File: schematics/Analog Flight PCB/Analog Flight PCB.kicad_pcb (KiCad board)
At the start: 2 copper layers, 77 parts, among them J1 Screw_Terminal_01x02, J10 Conn_01x02_Male, J2 Screw_Terminal_01x03, J3 Screw_Terminal_01x04, J4 Screw_Terminal_01x02, J5 Screw_Terminal_01x02, J6 Screw_Terminal_01x02, J7 Screw_Terminal_01x02, J8 Screw_Terminal_01x02, J9 Conn_02x06_Top_Bottom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

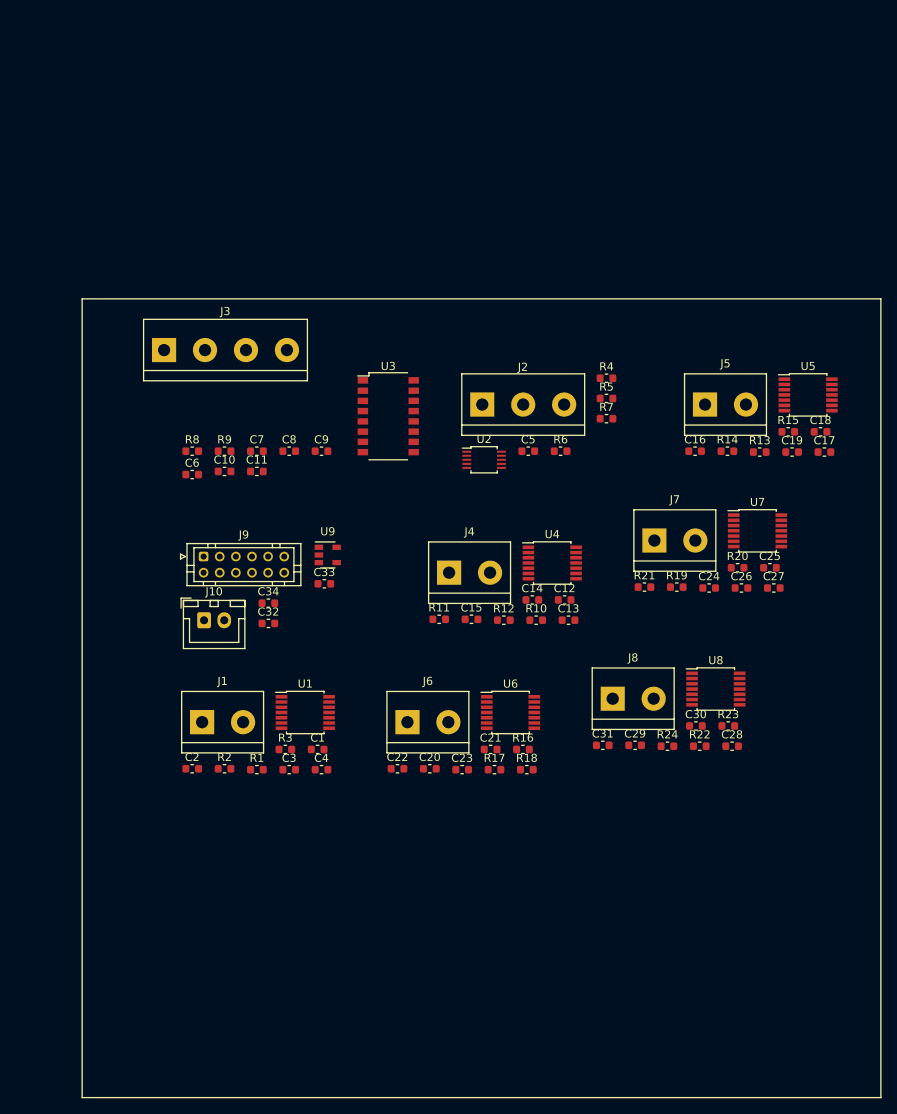
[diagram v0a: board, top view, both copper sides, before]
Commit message: Separated all components to make traces easier.
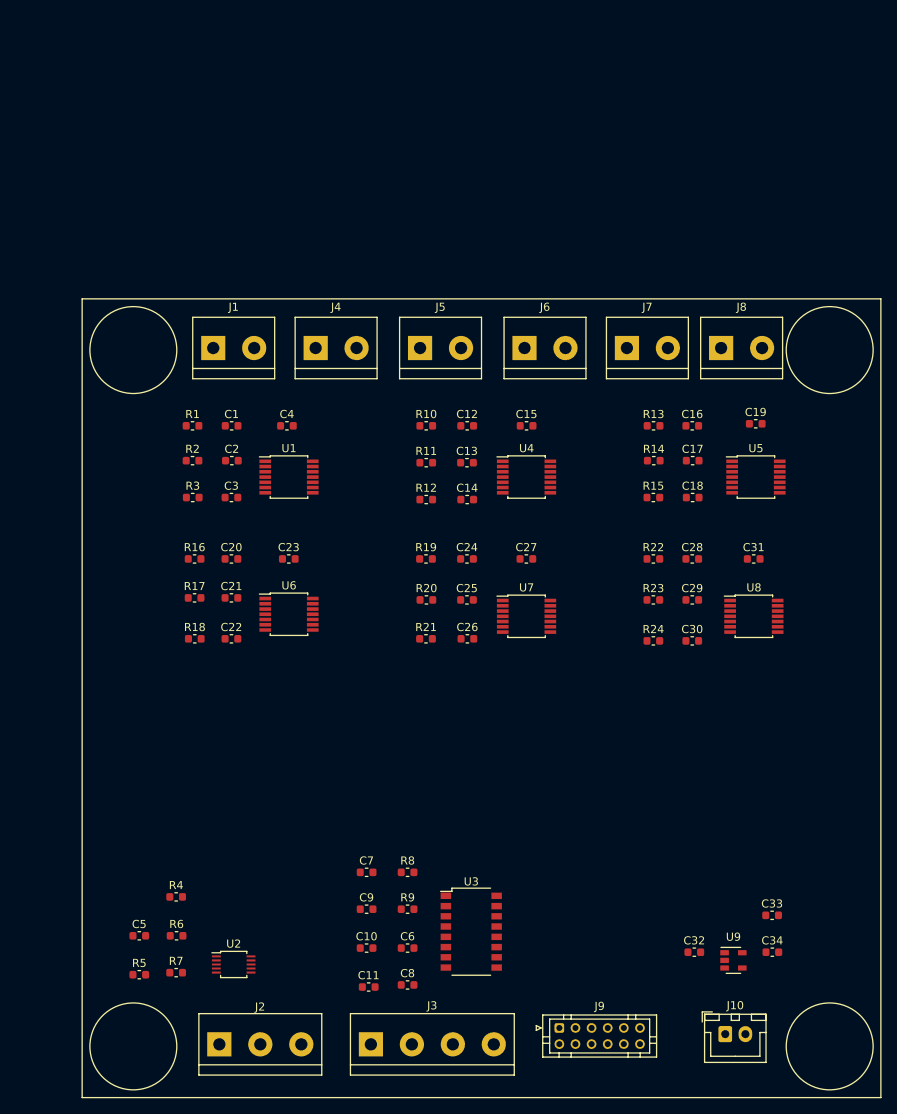
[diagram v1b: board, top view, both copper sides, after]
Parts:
- moved R5 92.0 mm to (108.7, 147.3)
- moved J3 89.8 mm to (137.4, 156.0)
- moved R7 87.0 mm to (113.3, 147.1)
- moved J2 85.8 mm to (118.6, 156.0)
- moved R4 83.6 mm to (113.3, 137.7)
- moved J10 82.5 mm to (181.4, 154.7)
- moved C5 77.1 mm to (108.7, 142.5)
- moved R6 76.7 mm to (113.3, 142.5)
- moved C34 76.0 mm to (187.2, 144.5)
- moved J9 73.2 mm to (160.8, 153.9)
- moved U9 71.1 mm to (182.4, 145.5)
- moved U2 69.9 mm to (120.4, 146.1)
- moved C33 69.1 mm to (187.2, 140.0)
- moved C8 67.8 mm to (142.0, 148.6)
- moved C32 66.7 mm to (177.5, 144.5)
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
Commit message: Changed screw terminals to JST connectors and added two more connectors to the PTs.
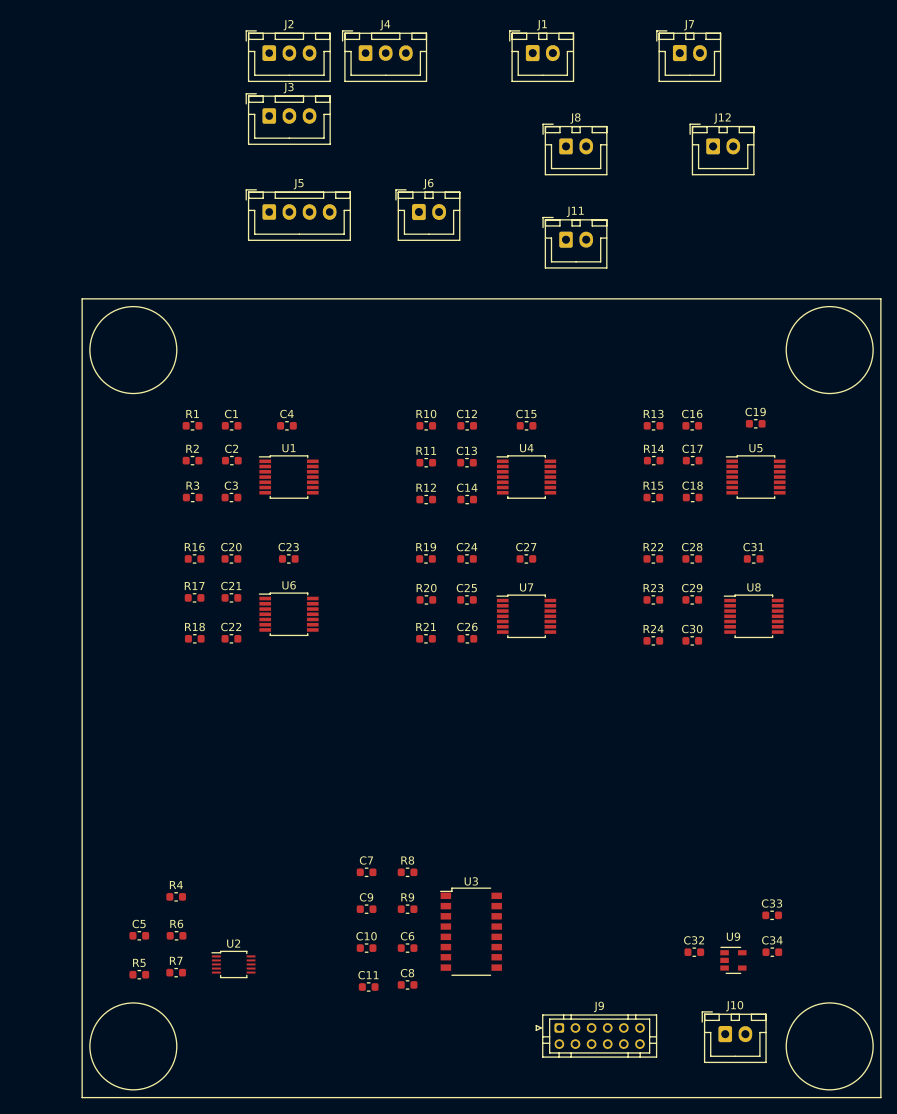
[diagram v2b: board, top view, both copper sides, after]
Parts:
- added J11: Conn_01x02_Male, Connector_JST:JST_XH_B2B-XH-A_1x02_P2.50mm_Vertical, F.Cu at (161.6, 56.2)
- added J12: Conn_01x02_Male, Connector_JST:JST_XH_B2B-XH-A_1x02_P2.50mm_Vertical, F.Cu at (179.8, 44.6)
- J1, J6, J7, J8: value Screw_Terminal_01x02 -> Conn_01x02_Male; footprint TerminalBlock:TerminalBlock_bornier-2_P5.08mm -> Connector_JST:JST_XH_B2B-XH-A_1x02_P2.50mm_Vertical
- J2: value Screw_Terminal_01x03 -> Conn_01x03_Male; footprint TerminalBlock:TerminalBlock_bornier-3_P5.08mm -> Connector_JST:JST_XH_B3B-XH-A_1x03_P2.50mm_Vertical
- J3: value Screw_Terminal_01x04 -> Conn_01x03_Male; footprint TerminalBlock:TerminalBlock_bornier-4_P5.08mm -> Connector_JST:JST_XH_B3B-XH-A_1x03_P2.50mm_Vertical
- J4: value Screw_Terminal_01x02 -> Conn_01x03_Male; footprint TerminalBlock:TerminalBlock_bornier-2_P5.08mm -> Connector_JST:JST_XH_B3B-XH-A_1x03_P2.50mm_Vertical
- J5: value Screw_Terminal_01x02 -> Conn_01x04_Male; footprint TerminalBlock:TerminalBlock_bornier-2_P5.08mm -> Connector_JST:JST_XH_B4B-XH-A_1x04_P2.50mm_Vertical
- moved J2 123.1 mm to (124.8, 33.0)
- moved J3 115.8 mm to (124.8, 40.8)
- moved J1 53.9 mm to (157.5, 33.0)
- moved J7 37.2 mm to (175.7, 33.0)
- moved J4 37.1 mm to (136.8, 33.0)
- moved J8 31.5 mm to (161.6, 44.6)
- moved J5 25.2 mm to (124.8, 52.7)
- moved J6 21.4 mm to (143.4, 52.7)
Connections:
- J3 pad 1: Net-(C11-Pad1) -> Net-(J2-Pad1)
- J3 pad 2: Net-(J3-Pad2) -> Net-(J2-Pad2)
- J3 pad 3: Net-(J3-Pad3) -> Net-(J2-Pad3)
- J4 pad 1: Net-(J4-Pad1) -> Net-(J2-Pad1)
- J4 pad 2: Net-(J4-Pad2) -> Net-(J2-Pad2)
- J5 pad 1: Net-(J5-Pad1) -> Net-(C11-Pad1)
- R10 pad 1: Net-(J4-Pad1) -> Net-(J6-Pad1)
- R11 pad 2: Net-(J4-Pad2) -> Net-(J6-Pad2)
- R12 pad 2: Net-(J4-Pad2) -> Net-(J6-Pad2)
- R13 pad 1: Net-(J5-Pad1) -> Net-(J7-Pad1)
- R14 pad 2: Net-(J5-Pad2) -> Net-(J7-Pad2)
- R15 pad 2: Net-(J5-Pad2) -> Net-(J7-Pad2)
- R16 pad 1: Net-(J6-Pad1) -> Net-(J8-Pad1)
- R17 pad 2: Net-(J6-Pad2) -> Net-(J8-Pad2)
- R18 pad 2: Net-(J6-Pad2) -> Net-(J8-Pad2)
- R19 pad 1: Net-(J7-Pad1) -> Net-(J11-Pad1)
- R20 pad 2: Net-(J7-Pad2) -> Net-(J11-Pad2)
- R21 pad 2: Net-(J7-Pad2) -> Net-(J11-Pad2)
- R22 pad 1: Net-(J8-Pad1) -> Net-(J12-Pad1)
- R23 pad 2: Net-(J8-Pad2) -> Net-(J12-Pad2)
- R24 pad 2: Net-(J8-Pad2) -> Net-(J12-Pad2)
- R8 pad 2: Net-(J3-Pad2) -> Net-(J5-Pad2)
- R9 pad 2: Net-(J3-Pad3) -> Net-(J5-Pad3)

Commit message: Finished layout for individual components and prepping for I2C and power connections.
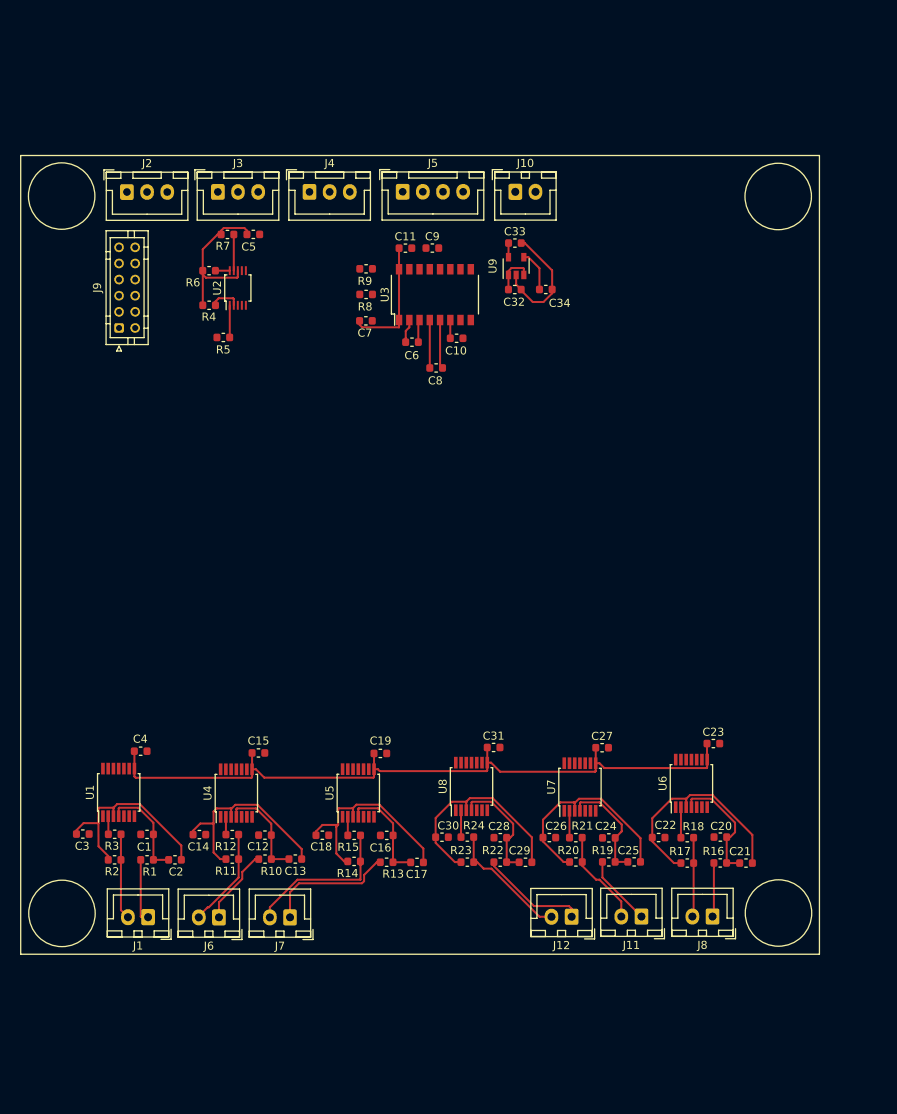
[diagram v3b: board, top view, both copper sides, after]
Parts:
- moved J7 117.6 mm to (127.4, 140.2), turned to 180 degrees
- moved J1 117.3 mm to (109.8, 140.2), turned to 180 degrees
- moved J10 107.7 mm to (155.3, 50.2)
- moved J9 102.6 mm to (106.2, 67.1), turned to 90 degrees
- moved J8 97.2 mm to (179.8, 140.1), turned to 180 degrees
- moved J12 97.1 mm to (162.3, 140.1), turned to 180 degrees
- moved R7 91.8 mm to (119.6, 55.5)
- moved C11 91.7 mm to (141.7, 57.2)
- moved J6 90.9 mm to (118.6, 140.2), turned to 180 degrees
- moved U9 90.2 mm to (155.4, 59.4), turned to 90 degrees
- moved C33 89.3 mm to (155.3, 56.6)
- moved C5 88.1 mm to (122.8, 55.5)
- moved C34 86.9 mm to (159.1, 62.3)
- moved C32 85.1 mm to (155.3, 62.3)
- moved J11 84.5 mm to (171.0, 140.1), turned to 180 degrees
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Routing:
- net +3V3: track 0.00 -> 112.3 mm
- net Net-(C21-Pad2): track 0.00 -> 27.8 mm
- net Net-(C17-Pad2): track 0.00 -> 26.9 mm
- net Net-(C29-Pad2): track 0.00 -> 26.4 mm
- net Net-(C25-Pad2): track 0.00 -> 26.2 mm
- net Net-(C13-Pad2): track 0.00 -> 26.2 mm
- net Net-(C2-Pad2): track 0.00 -> 25.9 mm
- net Net-(J7-Pad2): track 0.00 -> 19.4 mm
- net Net-(J7-Pad1): track 0.00 -> 16.4 mm
- net Net-(J12-Pad2): track 0.00 -> 15.6 mm
- net Net-(C11-Pad1): track 0.00 -> 15.3 mm
- net GND: track 0.00 -> 15.1 mm
- net Net-(C20-Pad2): track 0.00 -> 15.0 mm
- net Net-(C28-Pad2): track 0.00 -> 14.2 mm
- net Net-(C24-Pad2): track 0.00 -> 13.9 mm
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
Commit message: Preliminary PCB design for Analog Flight Board completed. Needs further review.
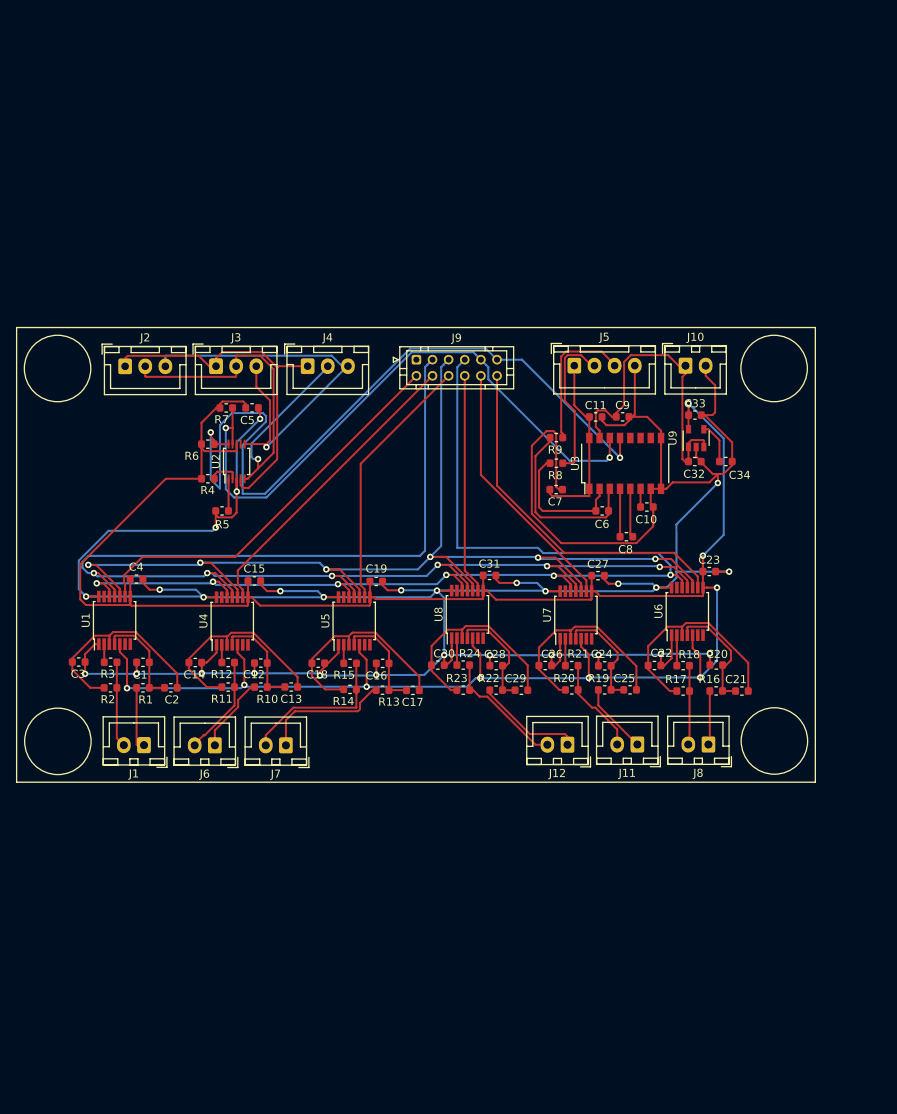
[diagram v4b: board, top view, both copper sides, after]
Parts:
- moved J9 37.1 mm to (143.1, 71.0), turned to 0 degrees
- moved C7 31.5 mm to (160.4, 87.2)
- moved U3 31.5 mm to (168.9, 83.9)
- moved C8 31.5 mm to (169.1, 93.0)
- moved R9 31.5 mm to (160.4, 80.7)
- moved R8 31.5 mm to (160.4, 83.9)
- moved C10 31.5 mm to (171.6, 89.3)
- moved C11 31.5 mm to (165.3, 78.1)
- moved C6 31.5 mm to (166.1, 89.8)
- moved C9 31.5 mm to (168.6, 78.1)
- moved C32 30.9 mm to (177.6, 83.7)
- moved U9 30.9 mm to (177.8, 80.8)
- moved C33 30.9 mm to (177.6, 77.9)
- moved C34 30.9 mm to (181.4, 83.7)
- moved J5 30.3 mm to (162.6, 71.8)
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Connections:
- J9 pad 1: /tc1/SCK -> Net-(J9-Pad1)
- J9 pad 10: /tc6/CS -> /tc5/CS
- J9 pad 12: /LC/SDA -> /tc4/CS
- J9 pad 2: /tc1/SDI -> /tc1/CS
- J9 pad 3: /tc1/CS -> /tc1/SDO
- J9 pad 5: /tc3/CS -> /tc1/SCK
- J9 pad 6: Net-(J9-Pad6) -> /tc3/CS
- J9 pad 7: /tc1/SDO -> /tc1/SDI
- J9 pad 8: /tc4/CS -> /tc6/CS
- J9 pad 9: /tc5/CS -> /LC/SDA
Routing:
- net GND: track 15.1 -> 418.4 mm, vias 0 -> 28
- net +3V3: track 112.3 -> 286.4 mm, vias 0 -> 9
- net /tc1/SDO: track 0.00 -> 170.3 mm, vias 0 -> 6
- net /tc1/SDI: track 0.00 -> 141.9 mm, vias 0 -> 6
- net /tc1/SCK: track 0.00 -> 137.8 mm, vias 0 -> 6
- net /LC/SCL: track 1.78 -> 98.4 mm, vias 0 -> 2
- net /LC/SDA: track 4.50 -> 77.5 mm, vias 0 -> 2
- net Net-(J2-Pad2): track 0.00 -> 53.0 mm, vias 0 -> 1
- net Net-(J2-Pad3): track 0.00 -> 52.3 mm, vias 0 -> 1
- net /tc1/CS: track 0.00 -> 49.2 mm
- net Net-(J2-Pad1): track 0.00 -> 44.8 mm
- net /tc4/CS: track 0.00 -> 44.6 mm
- net /tc2/CS: track 0.00 -> 37.7 mm
- net +5V: track 5.17 -> 39.8 mm
- net /tc3/CS: track 0.00 -> 32.2 mm
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
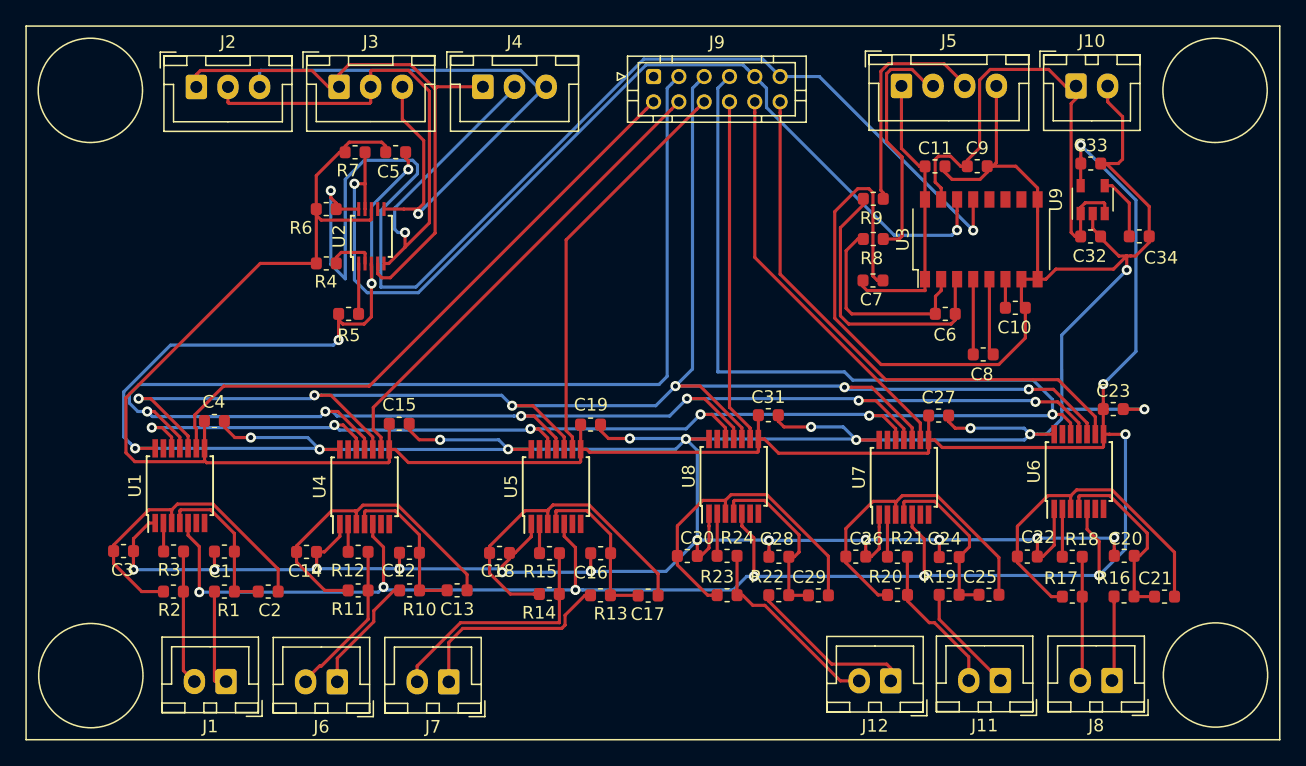
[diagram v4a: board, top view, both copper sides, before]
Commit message: ASPCB: Board cleanup
Fixed loadcell connection and cleaned up references. Also replaced silk
screen with edge cuts.
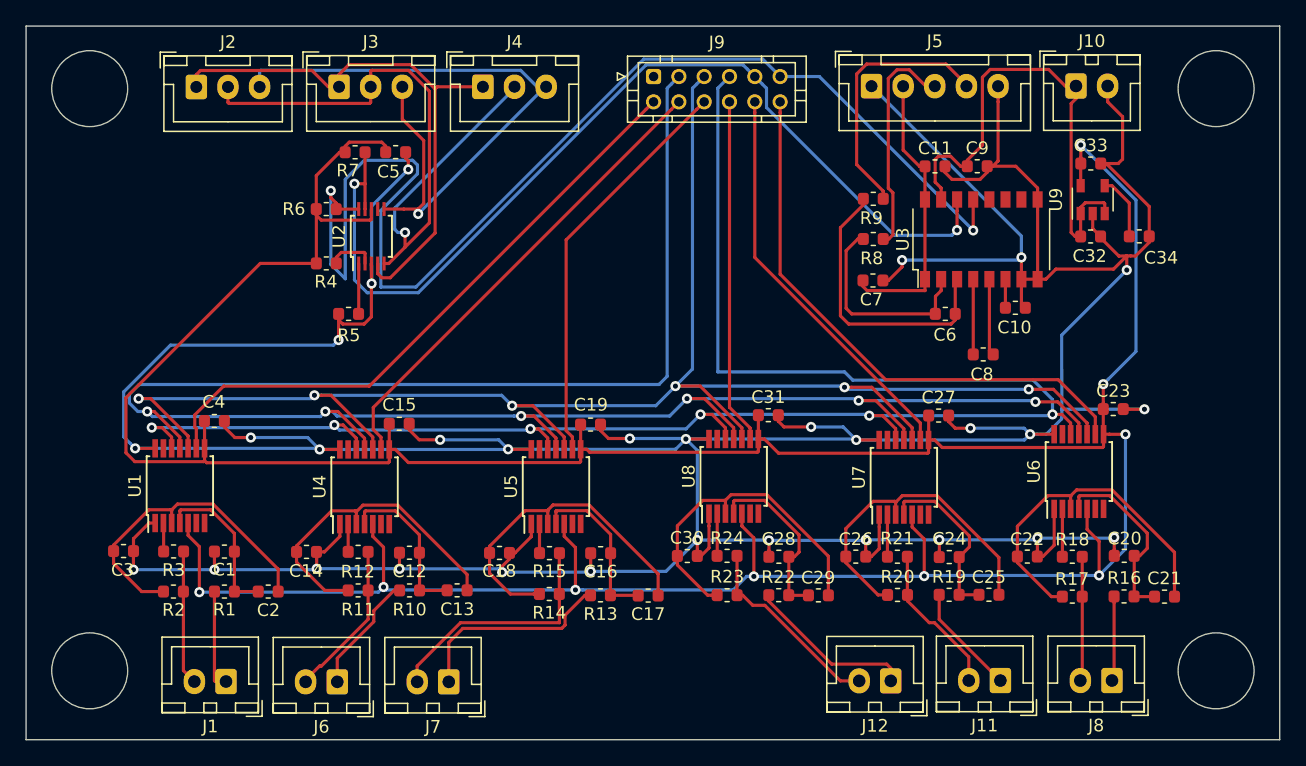
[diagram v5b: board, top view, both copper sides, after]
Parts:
- J5: value Conn_01x04_Male -> Conn_01x05_Male; footprint Connector_JST:JST_XH_B4B-XH-A_1x04_P2.50mm_Vertical -> Connector_JST:JST_XH_B5B-XH-A_1x05_P2.50mm_Vertical
- moved J5 2.36 mm to (160.3, 71.8)
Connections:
- J5 pad 1: Net-(C11-Pad1) -> GND
- J5 pad 2: Net-(J5-Pad2) -> Net-(C11-Pad1)
- J5 pad 4: GND -> Net-(J5-Pad4)
- R8 pad 2: Net-(J5-Pad2) -> Net-(J5-Pad3)
- R9 pad 2: Net-(J5-Pad3) -> Net-(J5-Pad4)
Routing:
- net Net-(J5-Pad4): track 0.00 -> 20.5 mm
- net Net-(J5-Pad2): track 19.8 -> 0.00 mm
- net GND: track 418.4 -> 410.9 mm, vias 28 -> 30
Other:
- board outline added: 99.1 x 56.4 mm
